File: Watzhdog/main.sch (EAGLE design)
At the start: 43 parts, among them CN1 MICROUSB(MC-5F-02), IC1 C8051F381-GM, IC3 N25Q512A, IC6 MPU-9250, U1 MCP73831, U2 TPS61201

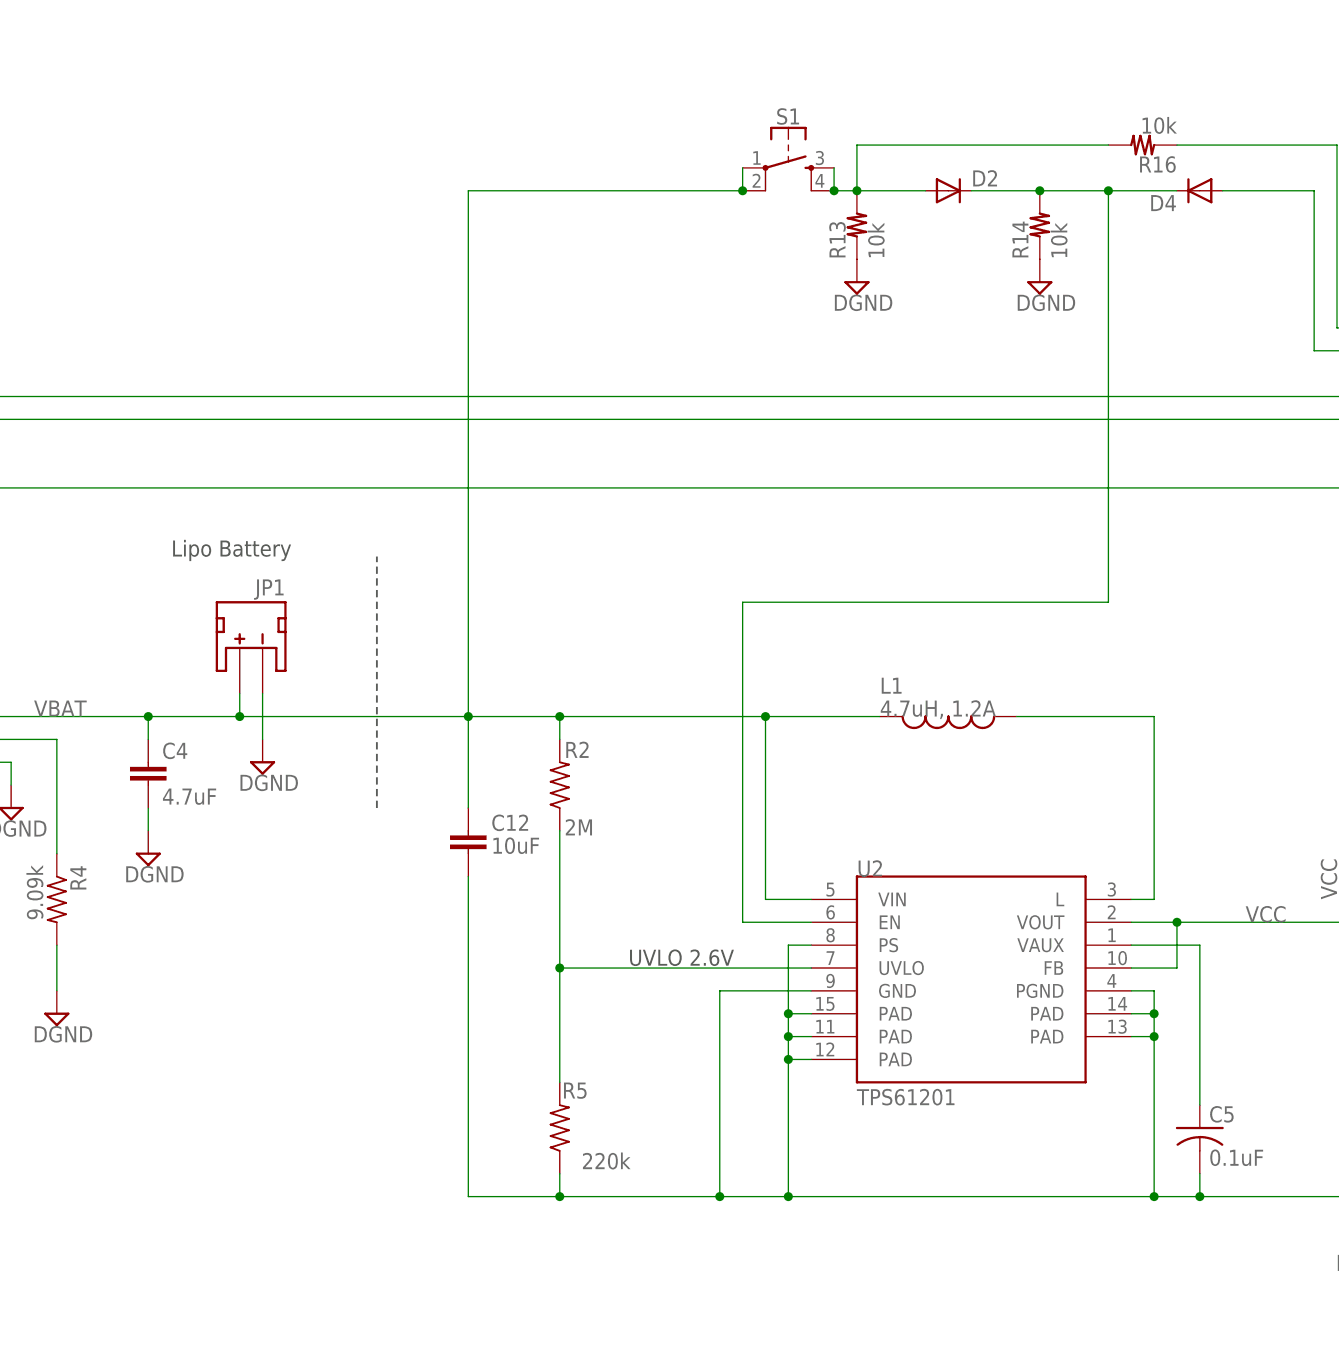
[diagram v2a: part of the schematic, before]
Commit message: Modified dc-dc converter curcuit
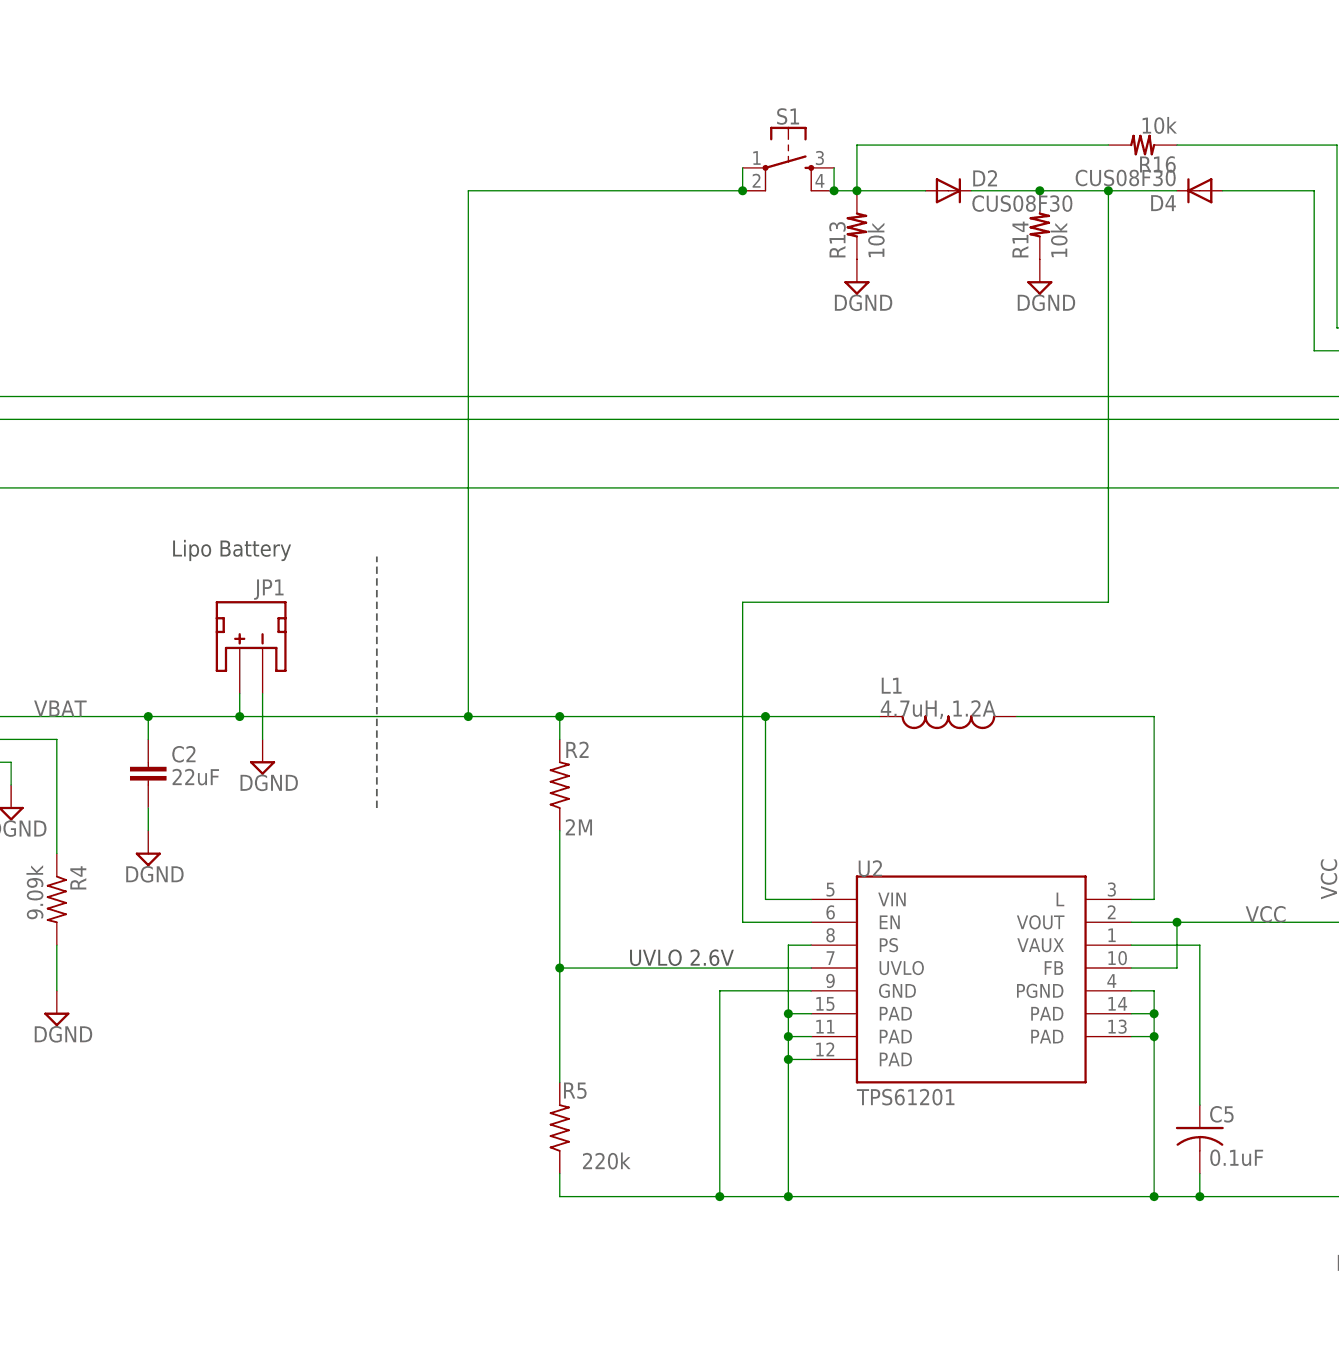
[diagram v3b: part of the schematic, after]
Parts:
- removed C12: 10uF, CH_passive:CAP1206
- removed C4: 4.7uF, SparkFun-Capacitors:4.7UF-6.3V-10%(0603)0603
- added C2: 22uF, CH_passive:CAP0805
- D2, D4: value (none) -> CUS08F30
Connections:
- net DGND: now also C2.2; no longer C12.2, C4.2
- net VBAT: now also C2.1; no longer C12.1, C4.1
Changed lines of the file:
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@@
 <part name="GND19" library="supply2" library_urn="urn:adsk.eagle:library:372" deviceset="DGND" device=""/>
 <part name="C3" library="SparkFun-Capacitors" deviceset="4.7UF-6.3V-10%(0603)" device="0603" value="4.7uF"/>
-<part name="C4" library="SparkFun-Capacitors" deviceset="4.7UF-6.3V-10%(0603)" device="0603" value="4.7uF"/>
 <part name="JP1" library="SparkFun-Connectors" deviceset="JST_2MM_MALE" device="" value="JST"/>
 <part name="C1" library="CH_passive" deviceset="CAP" device="0805" value="22uF"/>
@@
 <part name="R12" library="reg,cap" deviceset="R-" device="1005" value="100k"/>
 <part name="SUPPLY2" library="supply2" deviceset="DGND" device=""/>
-<part name="D2" library="diode" deviceset="DIODE-" device="SOD323-W"/>
-<part name="D4" library="diode" deviceset="DIODE-" device="SOD323-W"/>
+<part name="D2" library="diode" deviceset="DIODE-" device="SOD323-W" value="CUS08F30"/>
+<part name="D4" library="diode" deviceset="DIODE-" device="SOD323-W" value="CUS08F30"/>
 <part name="S1" library="SparkFun-Switches" deviceset="MOMENTARY-SWITCH-SPST-2" device="-SMD-4.6X2.8MM"/>
 <part name="GND2" library="supply2" library_urn="urn:adsk.eagle:library:372" deviceset="DGND" device=""/>
@@
 <part name="JP2" library="pinhead" library_urn="urn:adsk.eagle:library:325" deviceset="PINHD-1X1" device="" package3d_urn="urn:adsk.eagle:package:22485/2"/>
 <part name="JP3" library="pinhead" library_urn="urn:adsk.eagle:library:325" deviceset="PINHD-1X3" device="" package3d_urn="urn:adsk.eagle:package:22458/2"/>
-<part name="C12" library="CH_passive" deviceset="CAP" device="1206" value="10uF"/>
 <part name="CN1" library="Connector" deviceset="MICROUSB(MC-5F-02)" device=""/>
+<part name="C2" library="CH_passive" deviceset="CAP" device="0805" value="22uF"/>
 </parts>
 <sheets>
@@
 <instance part="GND19" gate="G$1" x="71.12" y="-10.16"/>
 <instance part="C3" gate="G$1" x="25.4" y="15.24"/>
-<instance part="C4" gate="G$1" x="81.28" y="15.24"/>
 <instance part="JP1" gate="G$1" x="93.98" y="30.48" rot="MR0"/>
 <instance part="C1" gate="G$1" x="215.9" y="-7.62" smashed="yes">
@@
 <instance part="JP2" gate="G$1" x="375.92" y="0" rot="R90"/>
 <instance part="JP3" gate="A" x="312.42" y="10.16" rot="R180"/>
-<instance part="C12" gate="G$1" x="116.84" y="7.62" smashed="yes">
-<attribute name="NAME" x="119.38" y="10.16" size="1.778" layer="95"/>
-<attribute name="VALUE" x="119.38" y="7.62" size="1.778" layer="96"/>
+<instance part="CN1" gate="G$1" x="0" y="17.78"/>
+<instance part="C2" gate="G$1" x="81.28" y="15.24" smashed="yes">
+<attribute name="NAME" x="83.82" y="17.78" size="1.778" layer="95"/>
+<attribute name="VALUE" x="83.82" y="15.24" size="1.778" layer="96"/>
 </instance>
-<instance part="CN1" gate="G$1" x="0" y="17.78"/>
 </instances>
 <busses>
@@
 <wire x1="127" y1="20.32" x2="127" y2="22.86" width="0.1524" layer="91"/>
 <wire x1="127" y1="22.86" x2="149.86" y2="22.86" width="0.1524" layer="91"/>
-<wire x1="116.84" y1="12.7" x2="116.84" y2="22.86" width="0.1524" layer="91"/>
 <wire x1="116.84" y1="22.86" x2="127" y2="22.86" width="0.1524" layer="91"/>
 <wire x1="162.56" y1="22.86" x2="149.86" y2="22.86" width="0.1524" layer="91"/>
@@
 <label x="68.58" y="22.86" size="1.778" layer="95"/>
 <pinref part="U1" gate="G$1" pin="VBAT"/>
-<pinref part="C4" gate="G$1" pin="1"/>
 <pinref part="JP1" gate="G$1" pin="+"/>
 <wire x1="116.84" y1="22.86" x2="91.44" y2="22.86" width="0.1524" layer="91"/>
@@
 <wire x1="147.32" y1="83.82" x2="147.32" y2="81.28" width="0.1524" layer="91"/>
 <junction x="147.32" y="81.28"/>
-<pinref part="C12" gate="G$1" pin="1"/>
+<pinref part="C2" gate="G$1" pin="1"/>
 </segment>
 </net>
@@
 <wire x1="81.28" y1="10.16" x2="81.28" y2="12.7" width="0.1524" layer="91"/>
 <pinref part="GND14" gate="G$1" pin="DGND"/>
-<pinref part="C4" gate="G$1" pin="2"/>
+<pinref part="C2" gate="G$1" pin="2"/>
 </segment>
 <segment>
@@
 <pinref part="U2" gate="G$1" pin="GND"/>
 <wire x1="198.12" y1="-27.94" x2="198.12" y2="-30.48" width="0.1524" layer="91"/>
-<wire x1="116.84" y1="5.08" x2="116.84" y2="-30.48" width="0.1524" layer="91"/>
-<wire x1="116.84" y1="-30.48" x2="127" y2="-30.48" width="0.1524" layer="91"/>
 <wire x1="127" y1="-30.48" x2="144.78" y2="-30.48" width="0.1524" layer="91"/>
 <wire x1="144.78" y1="-30.48" x2="152.4" y2="-30.48" width="0.1524" layer="91"/>
@@
 <pinref part="R5" gate="G$1" pin="1"/>
 <wire x1="127" y1="-27.94" x2="127" y2="-30.48" width="0.1524" layer="91"/>
-<junction x="127" y="-30.48"/>
 <wire x1="144.78" y1="-7.62" x2="144.78" y2="-30.48" width="0.1524" layer="91"/>
 <junction x="144.78" y="-30.48"/>
@@
 <wire x1="152.4" y1="-2.54" x2="152.4" y2="-10.16" width="0.1524" layer="91"/>
 <junction x="152.4" y="-10.16"/>
-<pinref part="C12" gate="G$1" pin="2"/>
-</segment>
-</net>
+</segment>
+</net>

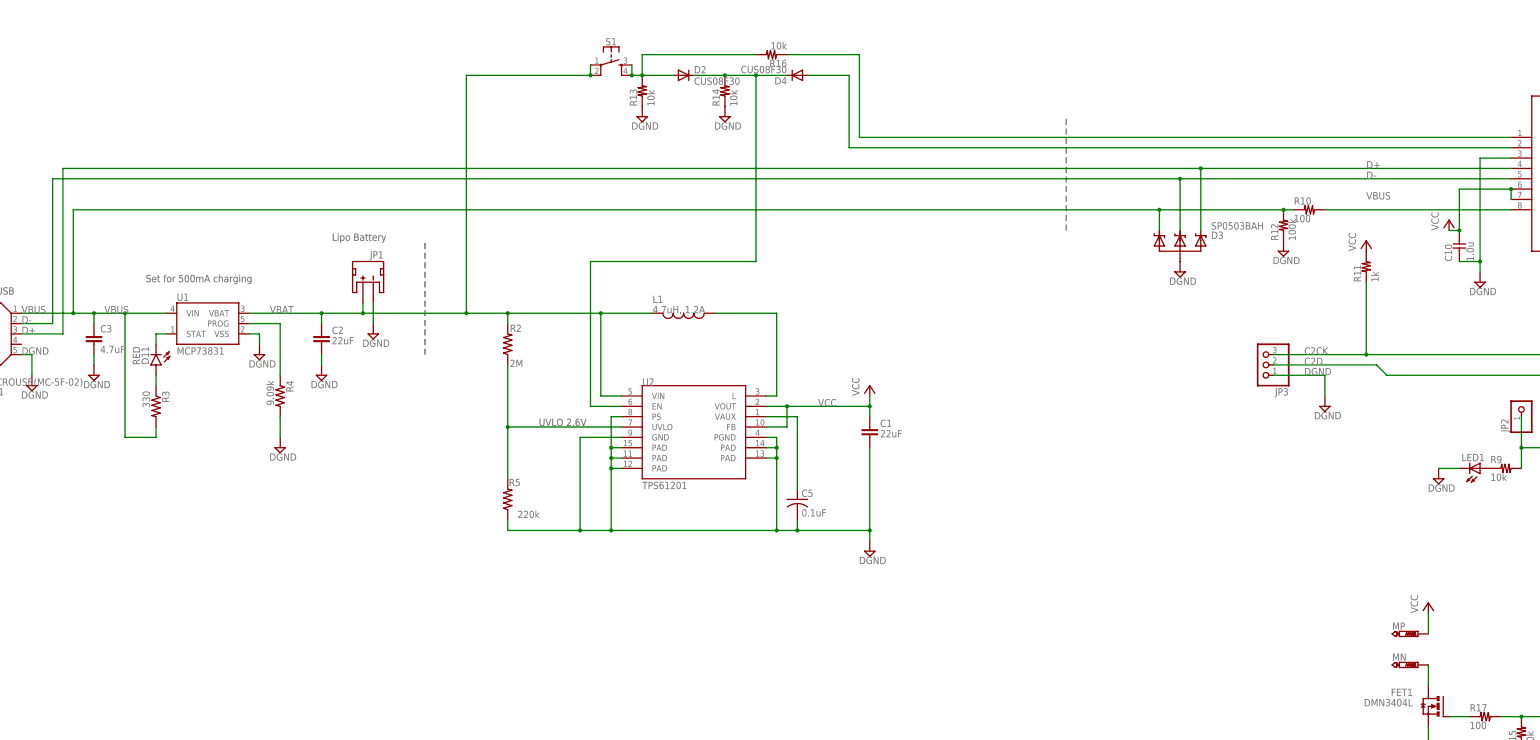
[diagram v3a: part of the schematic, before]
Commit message: Modified curcuit as a 2-layer board
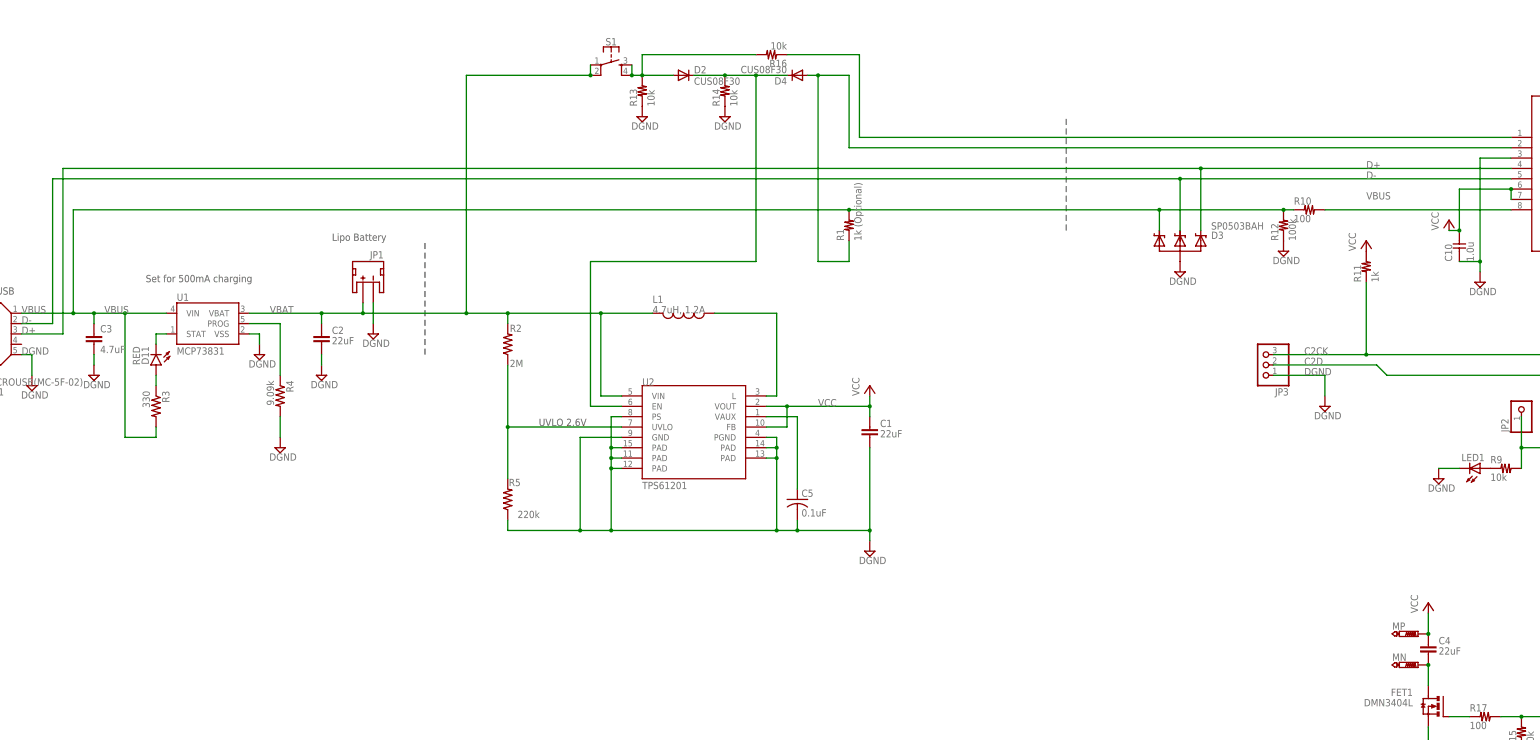
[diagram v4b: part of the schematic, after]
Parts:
- added C4: 22uF, CH_passive:CAP0805
- added R1: 1k (Optional), reg,cap:R-1005
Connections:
- net N$10: now also C4.2
- net N$7: now also R1.P$1
- net VBUS: now also R1.P$2
- net VCC: now also C4.1
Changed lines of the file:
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@@
 <part name="CN1" library="Connector" deviceset="MICROUSB(MC-5F-02)" device=""/>
 <part name="C2" library="CH_passive" deviceset="CAP" device="0805" value="22uF"/>
+<part name="R1" library="reg,cap" deviceset="R-" device="1005" value="1k (Optional)"/>
+<part name="C4" library="CH_passive" deviceset="CAP" device="0805" value="22uF"/>
 </parts>
 <sheets>
@@
 <attribute name="VALUE" x="83.82" y="15.24" size="1.778" layer="96"/>
 </instance>
+<instance part="R1" gate="G$1" x="210.82" y="43.18" rot="R90"/>
+<instance part="C4" gate="G$1" x="353.06" y="-60.96" smashed="yes">
+<attribute name="NAME" x="355.6" y="-58.42" size="1.778" layer="95"/>
+<attribute name="VALUE" x="355.6" y="-60.96" size="1.778" layer="96"/>
+</instance>
 </instances>
 <busses>
@@
 <pinref part="D3" gate="G$1" pin="4"/>
 <pinref part="R12" gate="G$1" pin="P$2"/>
-<wire x1="287.02" y1="48.26" x2="20.32" y2="48.26" width="0.1524" layer="91"/>
+<wire x1="287.02" y1="48.26" x2="210.82" y2="48.26" width="0.1524" layer="91"/>
+<wire x1="210.82" y1="48.26" x2="20.32" y2="48.26" width="0.1524" layer="91"/>
 <wire x1="40.64" y1="-5.08" x2="40.64" y2="-7.62" width="0.1524" layer="91"/>
 <wire x1="25.4" y1="20.32" x2="25.4" y2="22.86" width="0.1524" layer="91"/>
@@
 <pinref part="CN1" gate="G$1" pin="P$1"/>
 <label x="7.62" y="22.86" size="1.778" layer="95"/>
+<pinref part="R1" gate="G$1" pin="P$2"/>
+<junction x="210.82" y="48.26"/>
 </segment>
 </net>
@@
 <wire x1="353.06" y1="-55.88" x2="353.06" y2="-50.8" width="0.1524" layer="91"/>
 <pinref part="+3V3" gate="VCC" pin="VCC"/>
+<pinref part="C4" gate="G$1" pin="1"/>
+<junction x="353.06" y="-55.88"/>
 </segment>
 </net>
@@
 <wire x1="373.38" y1="63.5" x2="210.82" y2="63.5" width="0.1524" layer="91"/>
 <wire x1="210.82" y1="63.5" x2="210.82" y2="81.28" width="0.1524" layer="91"/>
-<wire x1="210.82" y1="81.28" x2="200.66" y2="81.28" width="0.1524" layer="91"/>
+<wire x1="210.82" y1="81.28" x2="203.2" y2="81.28" width="0.1524" layer="91"/>
 <pinref part="D4" gate="G$1" pin="A"/>
+<pinref part="R1" gate="G$1" pin="P$1"/>
+<wire x1="203.2" y1="81.28" x2="200.66" y2="81.28" width="0.1524" layer="91"/>
+<wire x1="210.82" y1="40.64" x2="210.82" y2="35.56" width="0.1524" layer="91"/>
+<wire x1="210.82" y1="35.56" x2="203.2" y2="35.56" width="0.1524" layer="91"/>
+<wire x1="203.2" y1="35.56" x2="203.2" y2="81.28" width="0.1524" layer="91"/>
+<junction x="203.2" y="81.28"/>
 </segment>
 </net>
@@
 <pinref part="FET1" gate="G$1" pin="D"/>
 <wire x1="353.06" y1="-63.5" x2="353.06" y2="-68.58" width="0.1524" layer="91"/>
-</segment>
-</net>
+<pinref part="C4" gate="G$1" pin="2"/>
+<junction x="353.06" y="-63.5"/>
+</segment>
+</net>
